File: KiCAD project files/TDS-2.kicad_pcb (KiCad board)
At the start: 2 copper layers, 52 x 100 mm, 22 parts, among them J1 Barrel_Jack_MountingPin, J2 Conn_01x03_Pin, J3 Conn_01x03_Pin, J4 Conn_01x03_Pin, J5 SN49B14B, J6 SN49B14B, U1 TL072

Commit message: Update
Updated the schematic, idk about the photos tho
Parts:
- removed J2, J3, J4: Conn_01x03_Pin, Connector_PinHeader_2.54mm:PinHeader_1x03_P2.54mm_Vertical
- added D2: 1N4007, Diode_THT:D_DO-41_SOD81_P10.16mm_Horizontal, F.Cu at (149.9, 114.0)
- added D3: 1N4007, Diode_THT:D_DO-41_SOD81_P10.16mm_Horizontal, F.Cu at (160.1, 110.7)
- added FTSW1: ~, Library:3PDT Footswitch, F.Cu at (143.3, 125.0)
- added R8: 1kΩ, Resistor_THT:R_Axial_DIN0207_L6.3mm_D2.5mm_P10.16mm_Horizontal, F.Cu at (153.6, 66.1)
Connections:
- C2 pad 1: Net-(J3-Pin_1) -> dst in
- RV2 pad 2: Net-(J4-Pin_1) -> dst out
- RV2 pad 3: GNDREF -> Net-(R8-Pad2)
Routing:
- net GNDREF: track 0.00 -> 105.2 mm
- net dst out: track 0.00 -> 77.5 mm
- net Net-(J4-Pin_1): track 73.7 -> 0.00 mm
- net out: track 53.9 -> 70.3 mm
- net dst in: track 0.00 -> 15.7 mm
- net Net-(D2-A): track 45.8 -> 59.4 mm
- net Net-(J3-Pin_1): track 9.29 -> 0.00 mm
- net GND: track 84.5 -> 90.6 mm
- net Net-(R8-Pad2): track 0.00 -> 4.36 mm
- net Net-(U1A-+): track 11.7 -> 14.5 mm
- net in: track 39.9 -> 41.8 mm
- net +9V: track 72.5 -> 71.9 mm
- net bypass: track 4.15 -> 4.70 mm
- removed copper zone on B.Cu, net GNDREF
- removed copper zone on F.Cu, net GNDREF
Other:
- board text removed: "Footswitch"

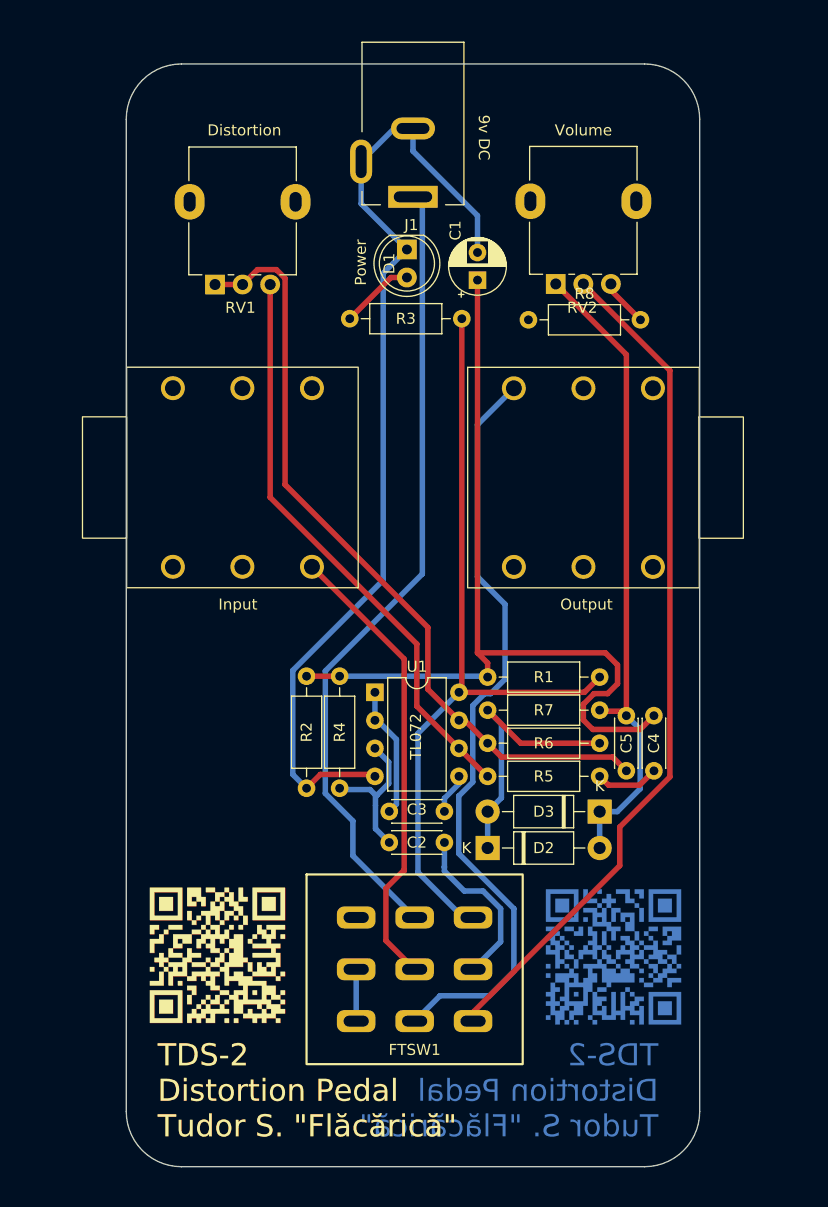
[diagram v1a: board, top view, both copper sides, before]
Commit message: Update
I updated the schematic PDF and the photo renders of the board
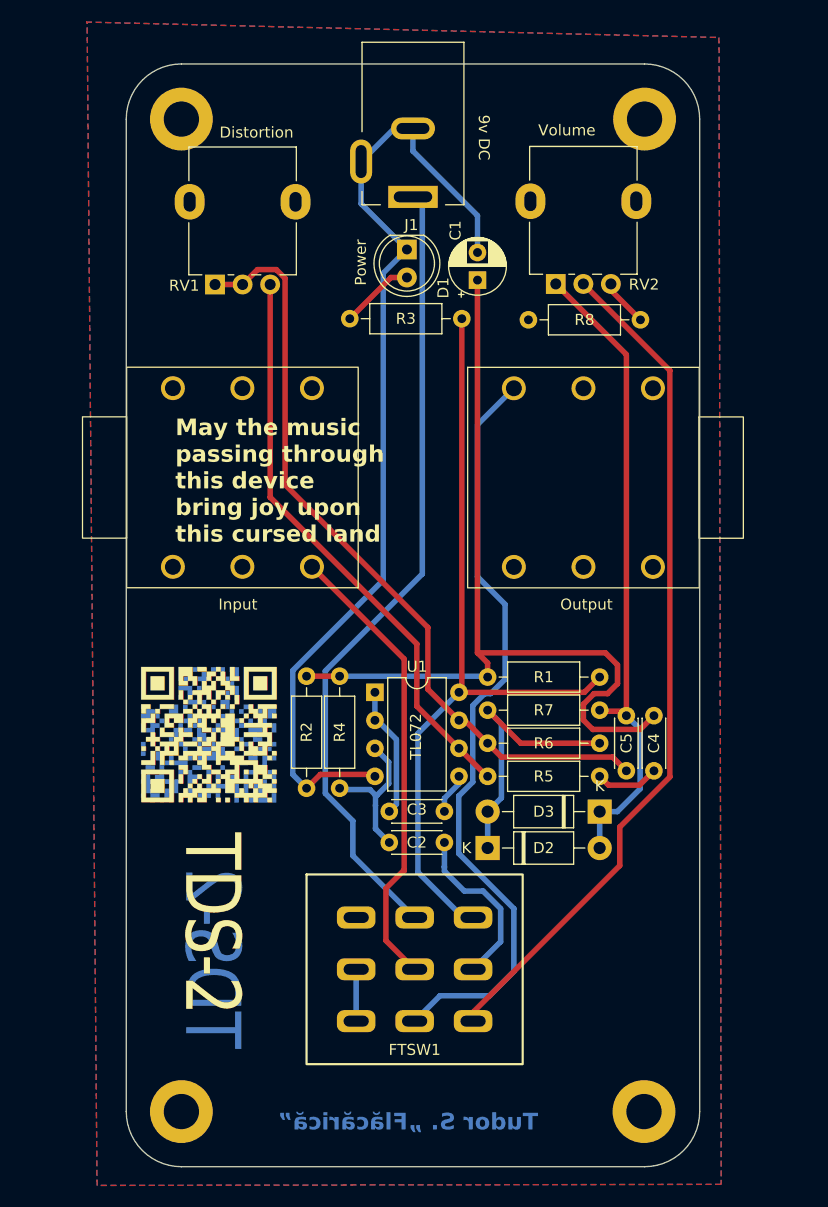
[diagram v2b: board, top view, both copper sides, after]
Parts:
- added ?: , , F.Cu at (164.2, 47.9)
- added ?: , , F.Cu at (122.2, 47.9)
- added ?: , , F.Cu at (122.2, 137.9)
- added ?: , , F.Cu at (164.1, 137.9)
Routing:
- added copper zone on B.Cu, net GNDREF
- added copper zone on F.Cu, net GNDREF
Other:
- board text added: "May the music passing through this device bring joy upon this cursed land"
- board text added: "TDS-2"
- board text added: "Tudor S. „Flăcărică”"
- board text removed: "TDS-2 Distortion Pedal Tudor S. {dblquote}Flăcărică{dblquote}"
